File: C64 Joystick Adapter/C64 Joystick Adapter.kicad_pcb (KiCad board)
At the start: 2 copper layers, 81.3 x 40.6 mm, 16 parts, among them J1 Port 1, J2 Port 2, J3 C64 JoyKEY, M1 Mounting, M2 Mounting, M3 Mounting, M4 Mounting, SW1 RESET, SW2 MODE

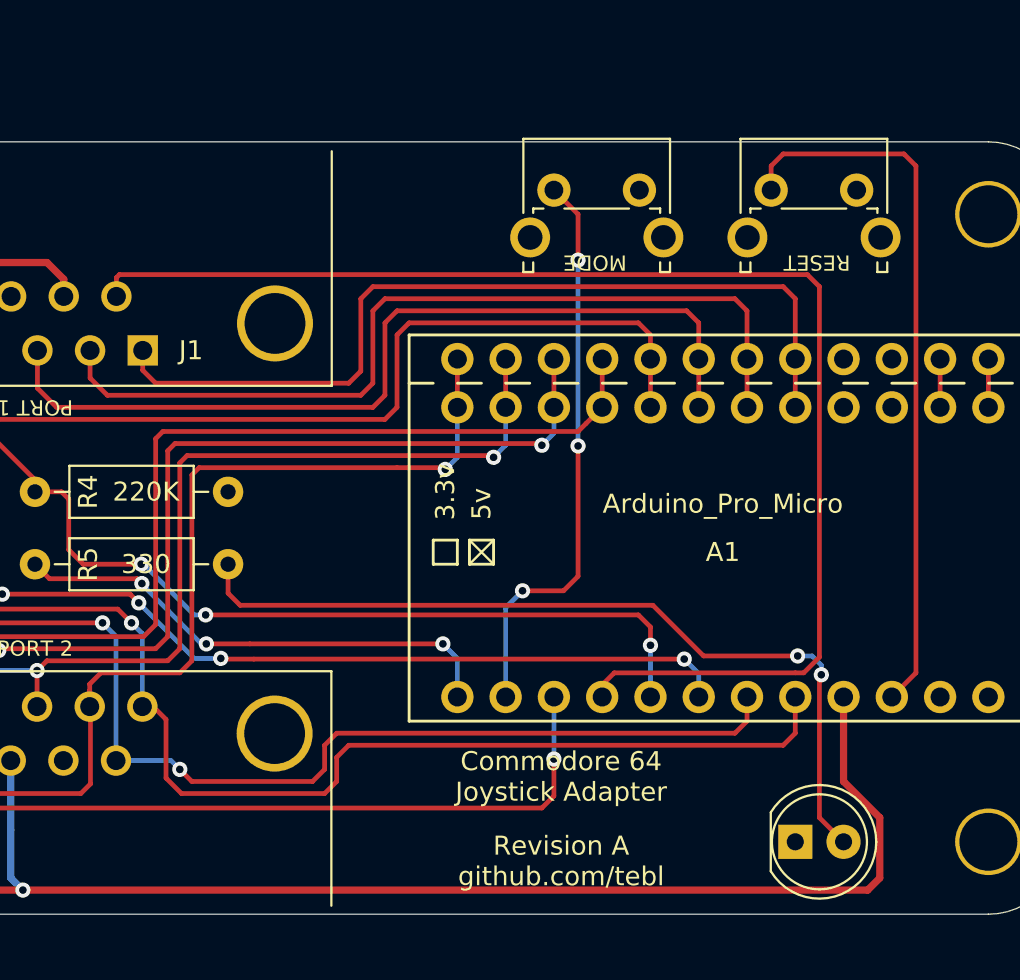
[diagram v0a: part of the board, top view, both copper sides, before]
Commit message: Changed SW1 footprint
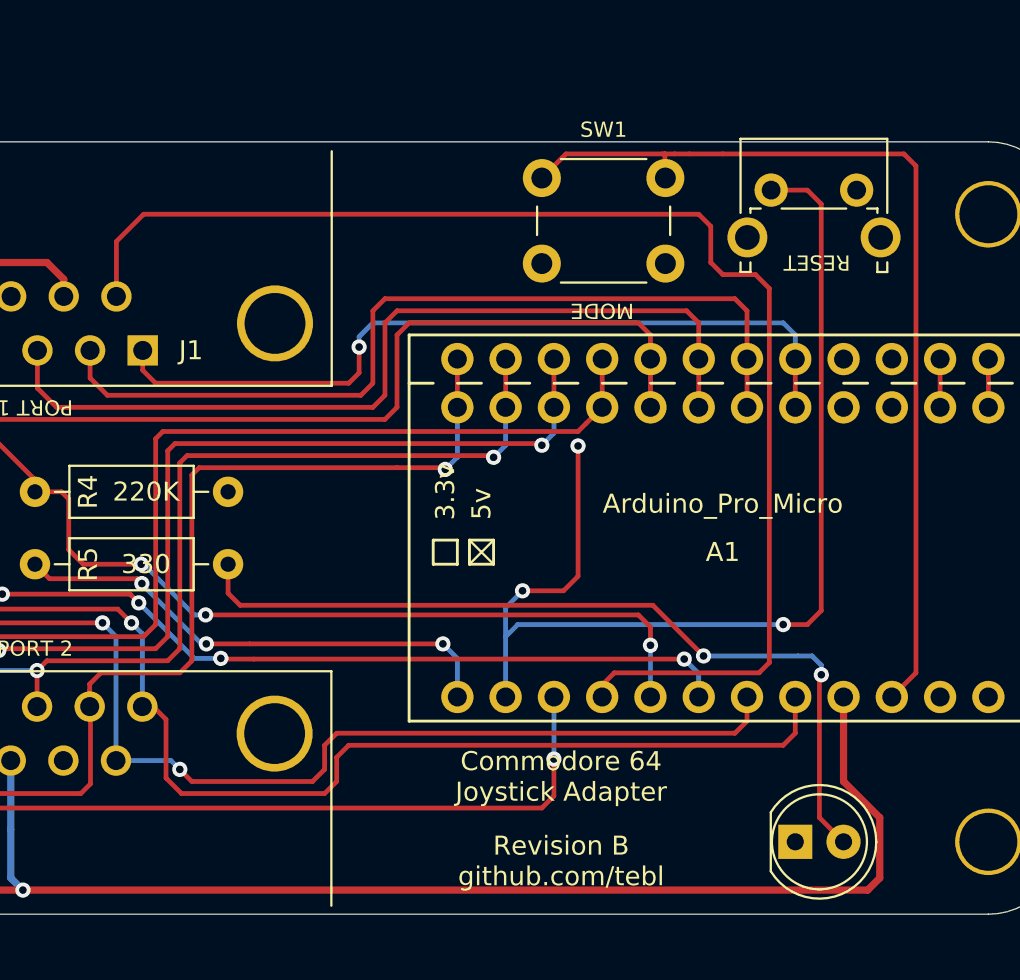
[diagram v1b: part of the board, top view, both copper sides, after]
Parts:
- SW1: footprint Button_Switch_THT:SW_Tactile_SPST_Angled_PTS645Vx39-2LFS -> Button_Switch_THT:SW_PUSH_6mm
- moved SW1 12.1 mm to (149.9, 73.7)
- moved SW2 11.4 mm to (161.9, 74.3)
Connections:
- A1 pad 24: Net-(A1-Pad24) -> (no net)
- J3 pad 10: Net-(J3-Pad10) -> (no net)
- M1 pad 1: Net-(M1-Pad1) -> (no net)
- M2 pad 1: Net-(M2-Pad1) -> (no net)
- M3 pad 1: Net-(M3-Pad1) -> (no net)
- M4 pad 1: Net-(M4-Pad1) -> (no net)
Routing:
- net Net-(A1-Pad14): track 30.0 -> 57.6 mm
- net Net-(A1-Pad22): track 37.9 -> 50.2 mm
- net P1_UP: track 46.0 -> 42.2 mm, vias 0 -> 1
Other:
- board text added: "PWR"
- board text added: "Revision B github.com/tebl"
- board text removed: "Revision A github.com/tebl"
- board text removed: "SYS"

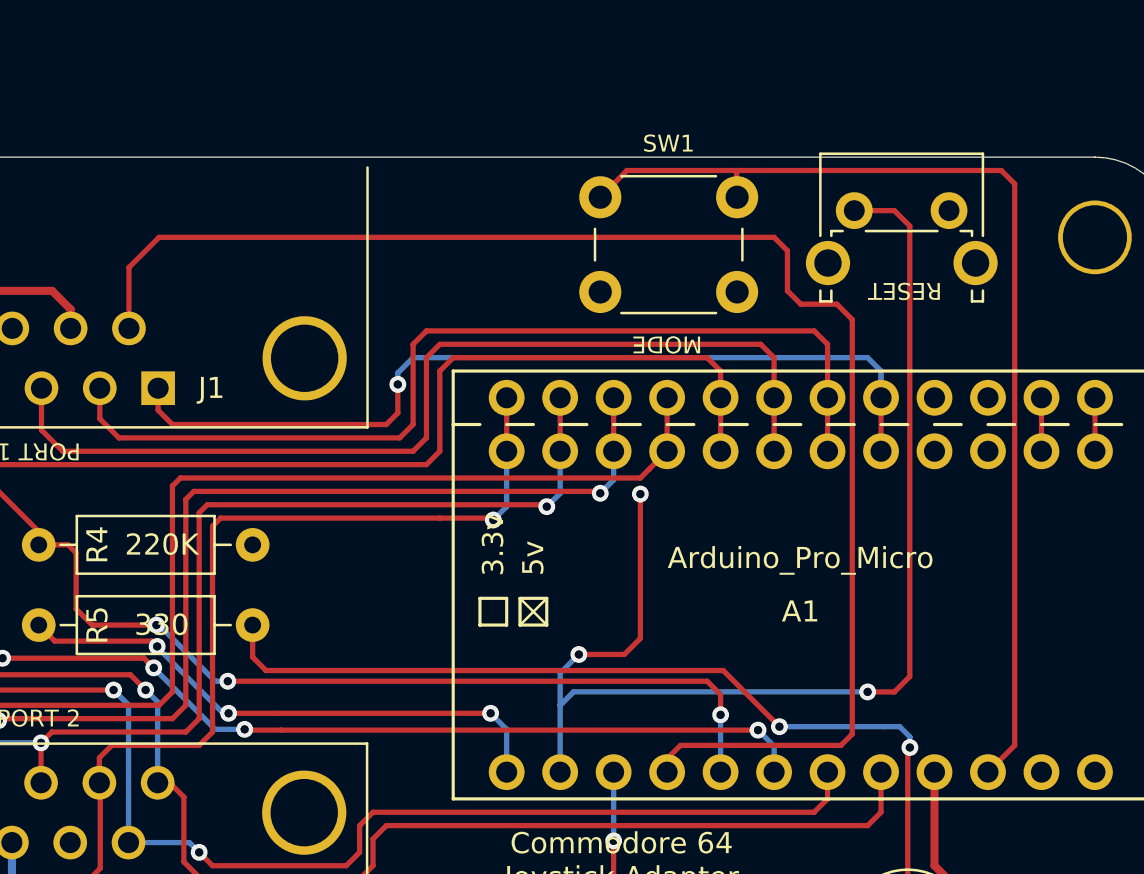
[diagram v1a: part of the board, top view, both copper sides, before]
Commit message: Blank faceplates and placement tweaks to main module
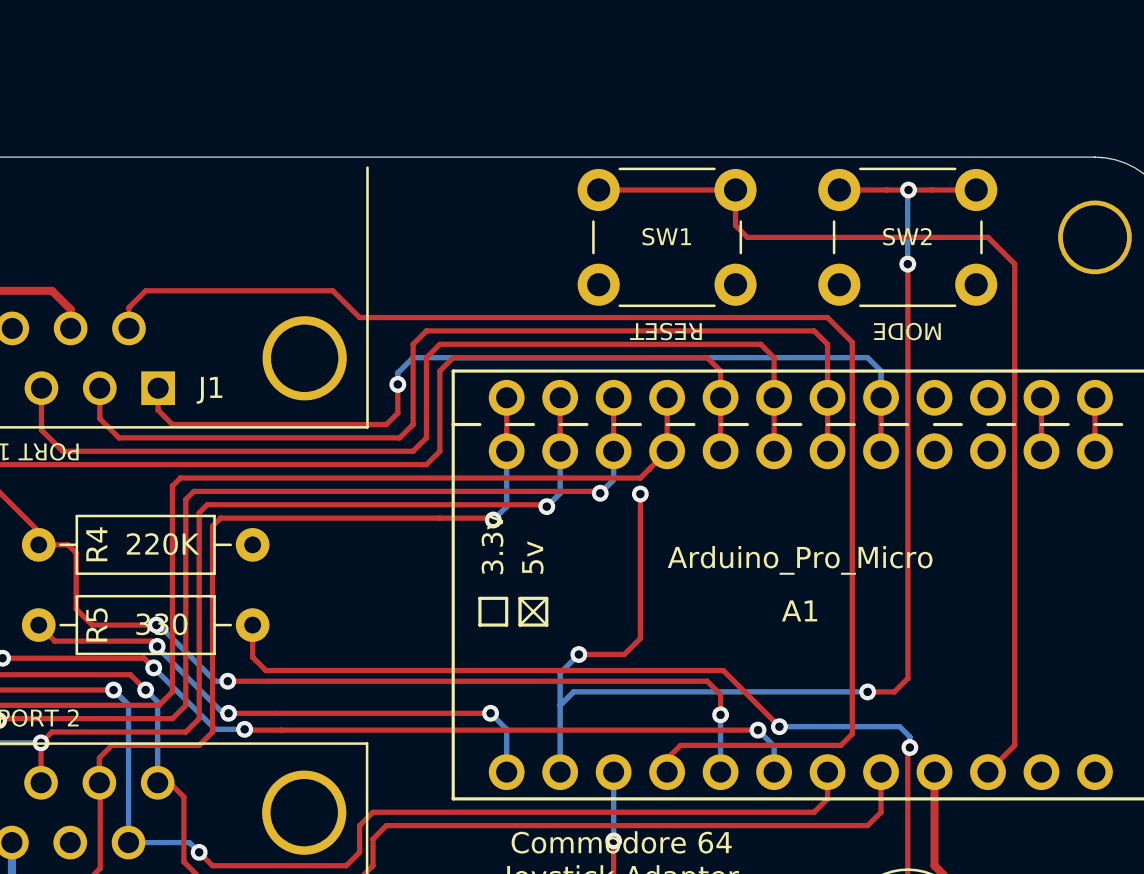
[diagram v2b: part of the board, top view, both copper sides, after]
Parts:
- SW1: footprint Button_Switch_THT:SW_PUSH_6mm -> switch_cutout:SW_PUSH_6mm
- SW2: footprint Button_Switch_THT:SW_Tactile_SPST_Angled_PTS645Vx39-2LFS -> switch_cutout:SW_PUSH_6mm
- moved SW1 3.70 mm to (153.0, 75.6)
- moved SW2 2.84 mm to (164.5, 75.6)
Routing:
- net Net-(A1-Pad14): track 57.6 -> 62.8 mm, vias 3 -> 5
- net P1_FIRE: track 70.2 -> 65.2 mm
- net Net-(A1-Pad22): track 50.2 -> 46.9 mm

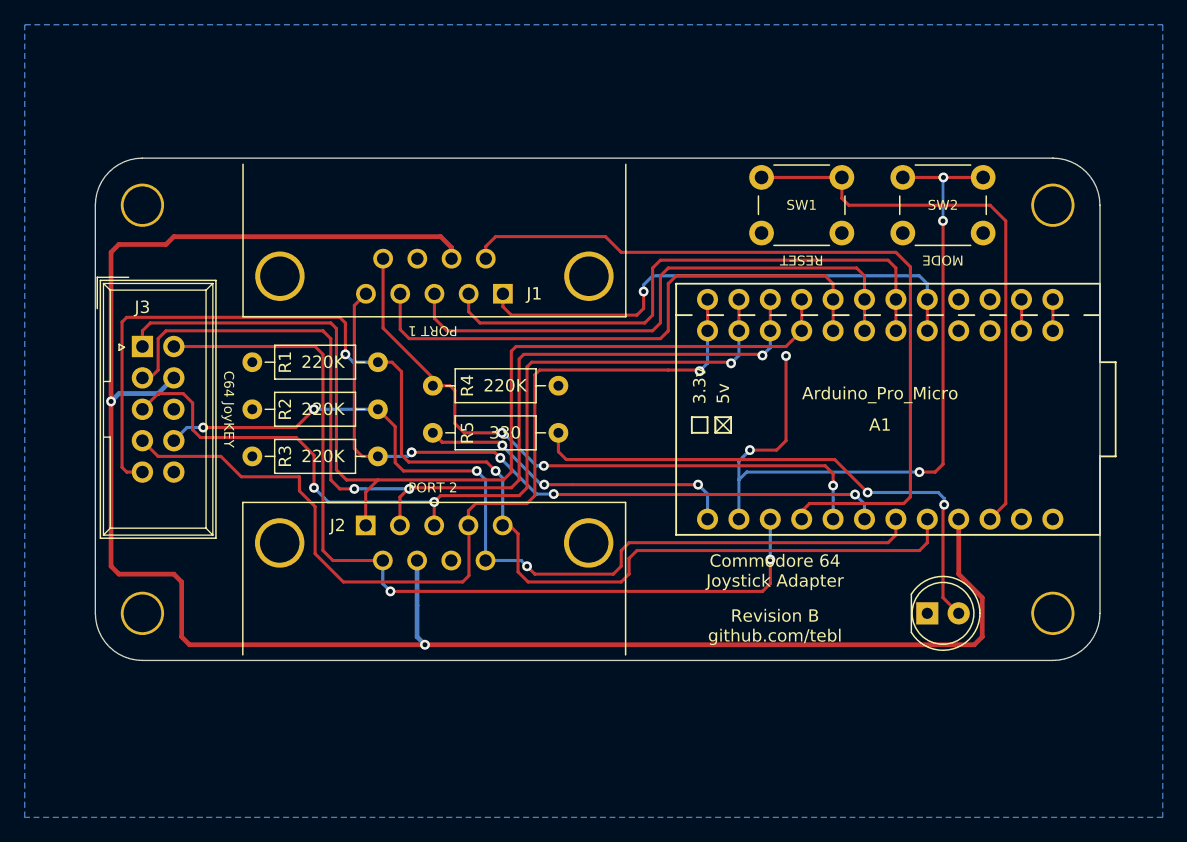
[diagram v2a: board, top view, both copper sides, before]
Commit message: Added jumpers for SEGA pinout
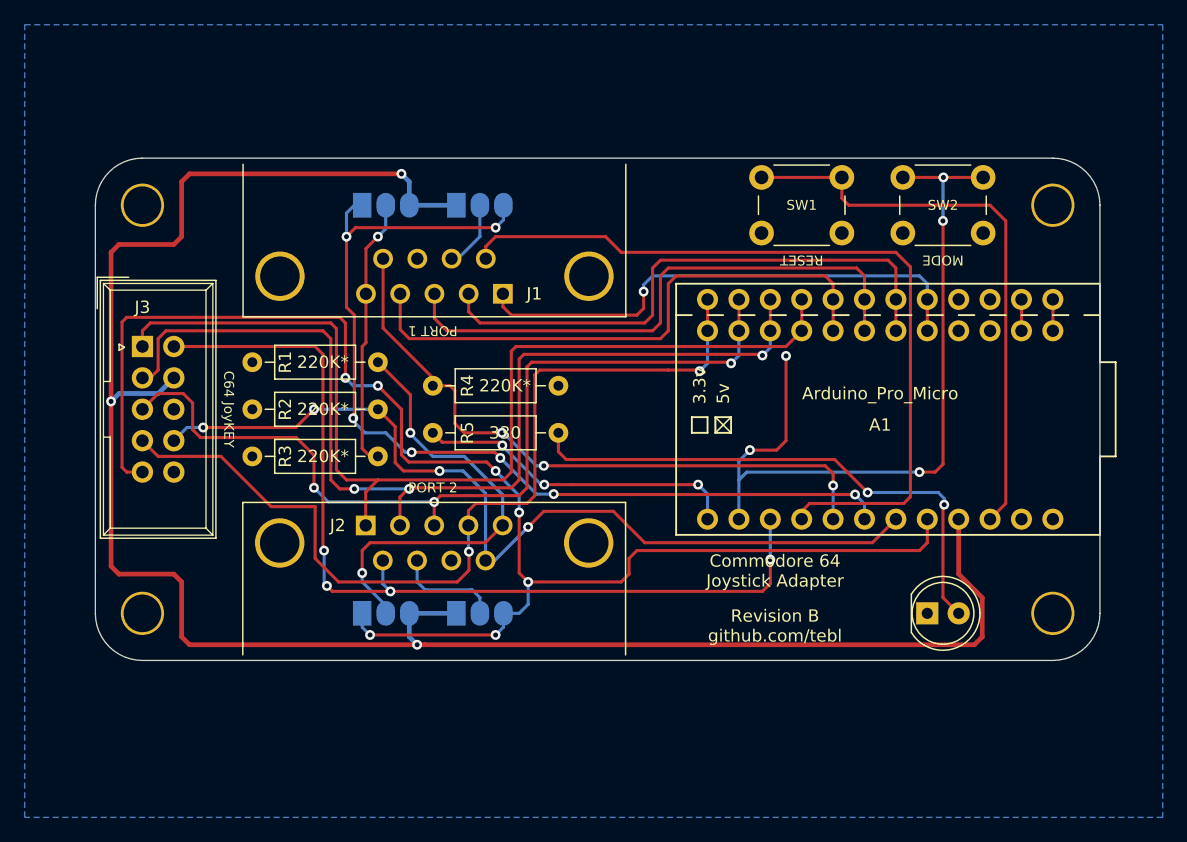
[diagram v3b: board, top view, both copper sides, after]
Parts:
- added JP1: SYSTEM, solder_bridge:select, B.Cu at (117.5, 108.6)
- added JP2: SYSTEM, solder_bridge:select2, B.Cu at (117.5, 75.6)
- added JP3: SYSTEM, solder_bridge:select, B.Cu at (125.1, 108.6)
- added JP4: SYSTEM, solder_bridge:select2, B.Cu at (125.1, 75.6)
- R1, R2, R3, R4: value 220K -> 220K*
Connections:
- J1 pad 5: POT_AY -> Net-(J1-Pad5)
- J1 pad 7: VCC -> Net-(J1-Pad7)
- J2 pad 5: POT_BY -> Net-(J2-Pad5)
- J2 pad 7: VCC -> Net-(J2-Pad7)
- R1 pad 2: POT_BY -> Net-(J2-Pad5)
- R3 pad 2: POT_AY -> Net-(J1-Pad5)
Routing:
- net Net-(J2-Pad5): track 0.00 -> 37.0 mm, vias 0 -> 2
- net Net-(J1-Pad5): track 0.00 -> 22.0 mm, vias 0 -> 1
- net POT_AY: track 57.5 -> 78.5 mm, vias 4 -> 7
- net POT_BY: track 101.2 -> 118.5 mm, vias 2 -> 7
- net Net-(J2-Pad7): track 0.00 -> 8.61 mm
- net Net-(J1-Pad7): track 0.00 -> 5.57 mm
- net VCC: track 154.0 -> 159.5 mm, vias 2 -> 3
- net P2_FIRE: track 72.3 -> 75.5 mm, vias 2 -> 4
- net POT_BX: track 73.9 -> 72.9 mm
- net P2_RIGHT: track 75.6 -> 75.0 mm, vias 1 -> 2
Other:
- board text added: "ATARI"

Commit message: Silkscreen tweaks
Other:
- board text added: "SEGA"
